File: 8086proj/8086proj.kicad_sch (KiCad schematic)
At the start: 1 part, among them U1 8086_Min_Mode

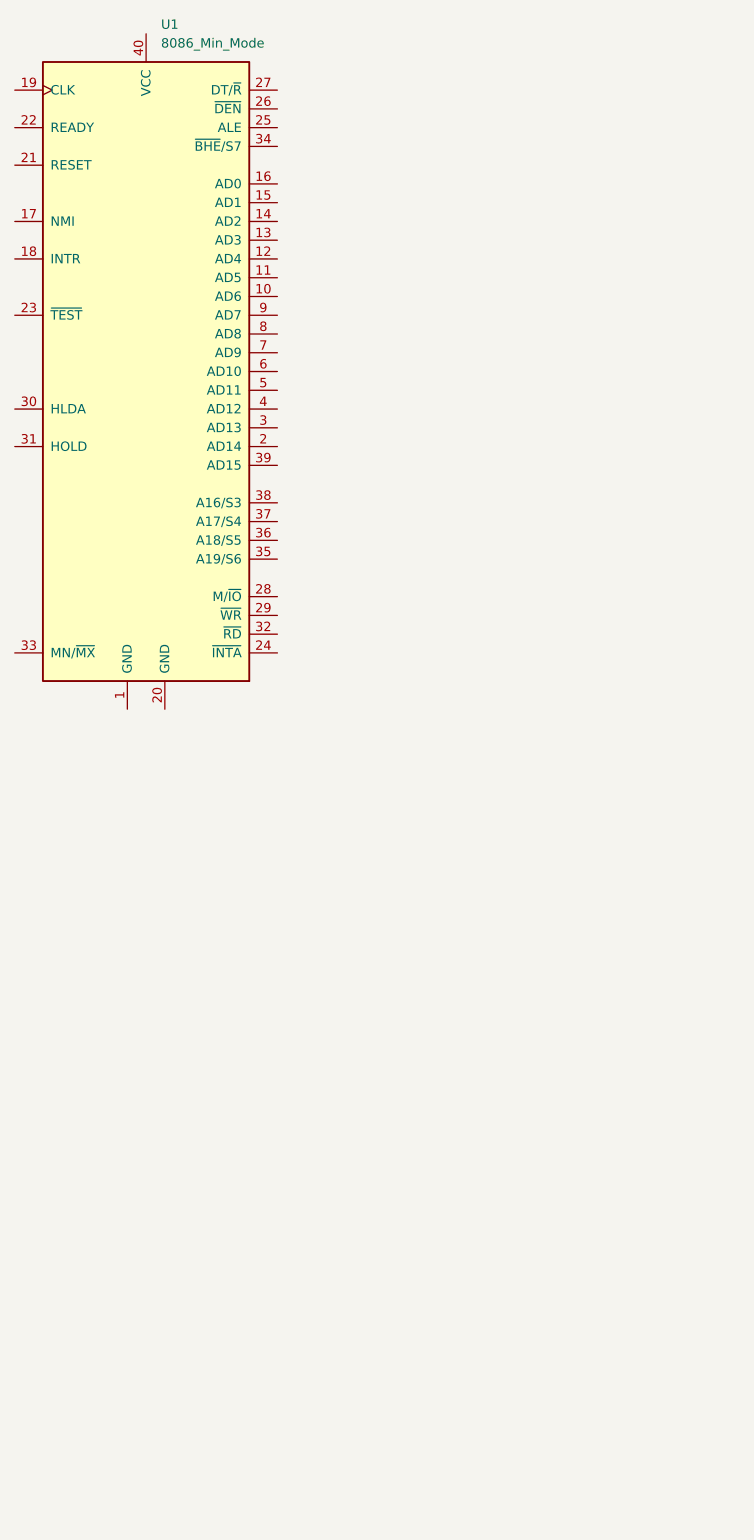
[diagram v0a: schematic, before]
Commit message: clock added
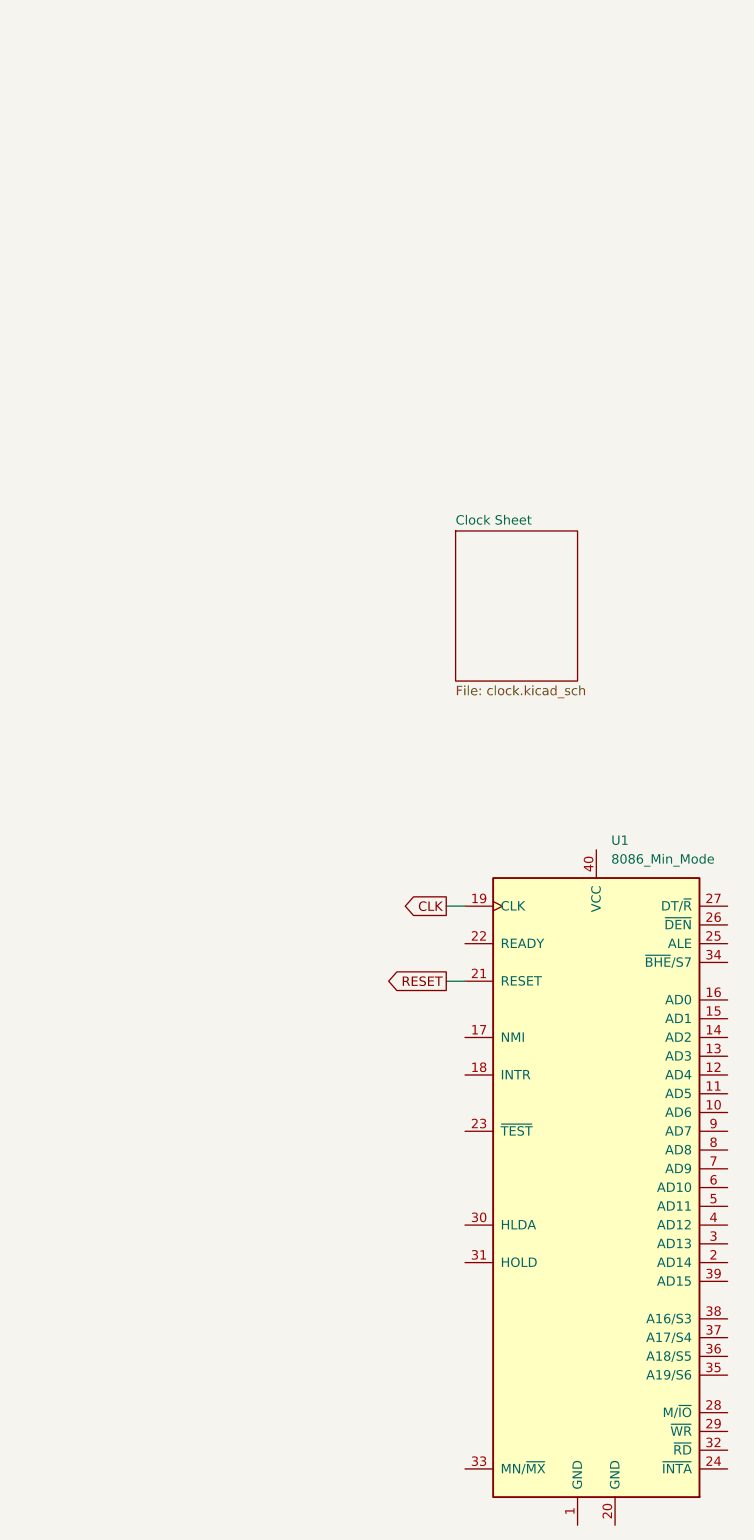
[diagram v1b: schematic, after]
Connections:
- net CLK: now reaches U1.19 (CLK)
- net RESET: now reaches U1.21 (RESET)
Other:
- added sheet Clock Sheet (clock.kicad_sch)
- moved on the sheet: U1
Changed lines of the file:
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@@
 (kicad_sch (version 20211123) (generator eeschema)
-  (paper "A4")
-  (symbol (lib_id "MCU_Intel:8086_Min_Mode") (at 113.03 97.79 0) (unit 1)
+  (paper "A2")
+  (wire (pts (xy 153.67 180.34) (xy 156.21 180.34))
+    (stroke (width 0) (type default) (color 0 0 0 0))
+  )
+  (wire (pts (xy 153.67 170.18) (xy 156.21 170.18))
+    (stroke (width 0) (type default) (color 0 0 0 0))
+  )
+  (global_label "CLK" (shape output) (at 153.67 170.18 180) (fields_autoplaced)
+    (effects (font (size 1.27 1.27)) (justify right))
+    (property "Intersheet References" "${INTERSHEET_REFS}" (id 0) (at 147.6888 170.2594 0)
+      (effects (font (size 1.27 1.27)) (justify right) hide)
+    )
+  )
+  (global_label "RESET" (shape output) (at 153.67 180.34 180) (fields_autoplaced)
+    (effects (font (size 1.27 1.27)) (justify right))
+    (property "Intersheet References" "${INTERSHEET_REFS}" (id 0) (at 145.5117 180.2606 0)
+      (effects (font (size 1.27 1.27)) (justify right) hide)
+    )
+  )
+  (symbol (lib_id "MCU_Intel:8086_Min_Mode") (at 173.99 208.28 0) (unit 1)
     (in_bom yes) (on_board yes) (fields_autoplaced)
-    (property "Reference" "U1" (id 0) (at 115.0494 50.8 0)
+    (property "Reference" "U1" (id 0) (at 176.0094 161.29 0)
       (effects (font (size 1.27 1.27)) (justify left))
     )
-    (property "Value" "8086_Min_Mode" (id 1) (at 115.0494 53.34 0)
+    (property "Value" "8086_Min_Mode" (id 1) (at 176.0094 163.83 0)
       (effects (font (size 1.27 1.27)) (justify left))
     )
-    (property "Footprint" "Package_DIP:DIP-40_W15.24mm" (id 2) (at 114.3 95.25 0)
+    (property "Footprint" "Package_DIP:DIP-40_W15.24mm" (id 2) (at 175.26 205.74 0)
       (effects (font (size 1.27 1.27) italic) hide)
     )
-    (property "Datasheet" "http://datasheets.chipdb.org/Intel/x86/808x/datashts/8086/231455-006.pdf" (id 3) (at 113.03 96.52 0)
+    (property "Datasheet" "http://datasheets.chipdb.org/Intel/x86/808x/datashts/8086/231455-006.pdf" (id 3) (at 173.99 207.01 0)
       (effects (font (size 1.27 1.27)) hide)
     )
@@
     (pin "9")
   )
+  (sheet (at 154.94 119.38) (size 16.51 20.32) (fields_autoplaced)
+    (stroke (width 0.1524) (type solid) (color 0 0 0 0))
+    (fill (color 0 0 0 0.0000))
+    (property "Sheet name" "Clock Sheet" (id 0) (at 154.94 118.6684 0)
+      (effects (font (size 1.27 1.27)) (justify left bottom))
+    )
+    (property "Sheet file" "clock.kicad_sch" (id 1) (at 154.94 140.2846 0)
+      (effects (font (size 1.27 1.27)) (justify left top))
+    )
+  )
   (sheet_instances
     (path "/" (page "1"))
+    (path "/4fad3d9c-9ad7-4272-a965-ec06eb9cc530" (page "2"))
   )
   (symbol_instances
+    (path "/4fad3d9c-9ad7-4272-a965-ec06eb9cc530/716f2b1a-b893-4511-a3ae-232edefae399"
+      (reference "#PWR?") (unit 1) (value "VCC") (footprint "")
+    )
+    (path "/4fad3d9c-9ad7-4272-a965-ec06eb9cc530/a658c771-b492-44ef-a949-143f5d3b159d"
+      (reference "#PWR?") (unit 1) (value "GND") (footprint "")
+    )
+    (path "/4fad3d9c-9ad7-4272-a965-ec06eb9cc530/c8dbae02-c6f8-4e68-b358-3a6c501e083a"
+      (reference "C?") (unit 1) (value "10uF") (footprint "")
+    )
+    (path "/4fad3d9c-9ad7-4272-a965-ec06eb9cc530/8f81149b-faae-4b3c-970a-6a2ac15a1b0c"
+      (reference "D?") (unit 1) (value "LED") (footprint "")
+    )
+    (path "/4fad3d9c-9ad7-4272-a965-ec06eb9cc530/440913ab-5556-4090-a89c-cd1fd9afe3ea"
+      (reference "R?") (unit 1) (value "10k") (footprint "")
+    )
+    (path "/4fad3d9c-9ad7-4272-a965-ec06eb9cc530/38675050-53ea-4ee8-8cd2-47093a802c56"
+      (reference "SW?") (unit 1) (value "SW_DIP_x01") (footprint "")
+    )
     (path "/174f9a27-35f7-4dde-a329-3ab5c39f6afc"
       (reference "U1") (unit 1) (value "8086_Min_Mode") (footprint "Package_DIP:DIP-40_W15.24mm")
     )
+    (path "/4fad3d9c-9ad7-4272-a965-ec06eb9cc530/55000a4c-19c7-458e-9166-3e8b2c45b34c"
+      (reference "U?") (unit 1) (value "8284") (footprint "Package_DIP:DIP-18_W7.62mm")
+    )
+    (path "/4fad3d9c-9ad7-4272-a965-ec06eb9cc530/6331dce3-1309-41e4-aca9-ad8e62dc2f98"
+      (reference "Y?") (unit 1) (value "Crystal") (footprint "")
+    )
   )
